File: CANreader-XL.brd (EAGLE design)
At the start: 99.8 x 49.8 mm, 101 parts, among them IC1 STM32F107RBT, IC2 TJA1055T/3, IC3 BD9G101G, IC4 LM1117IMPX-3.3, IC5 MCP2562-SOIC8, IC7 DP83848I, Q1 25MHz, SW1 SLEEP, SW2 TERM, U1 HC_05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

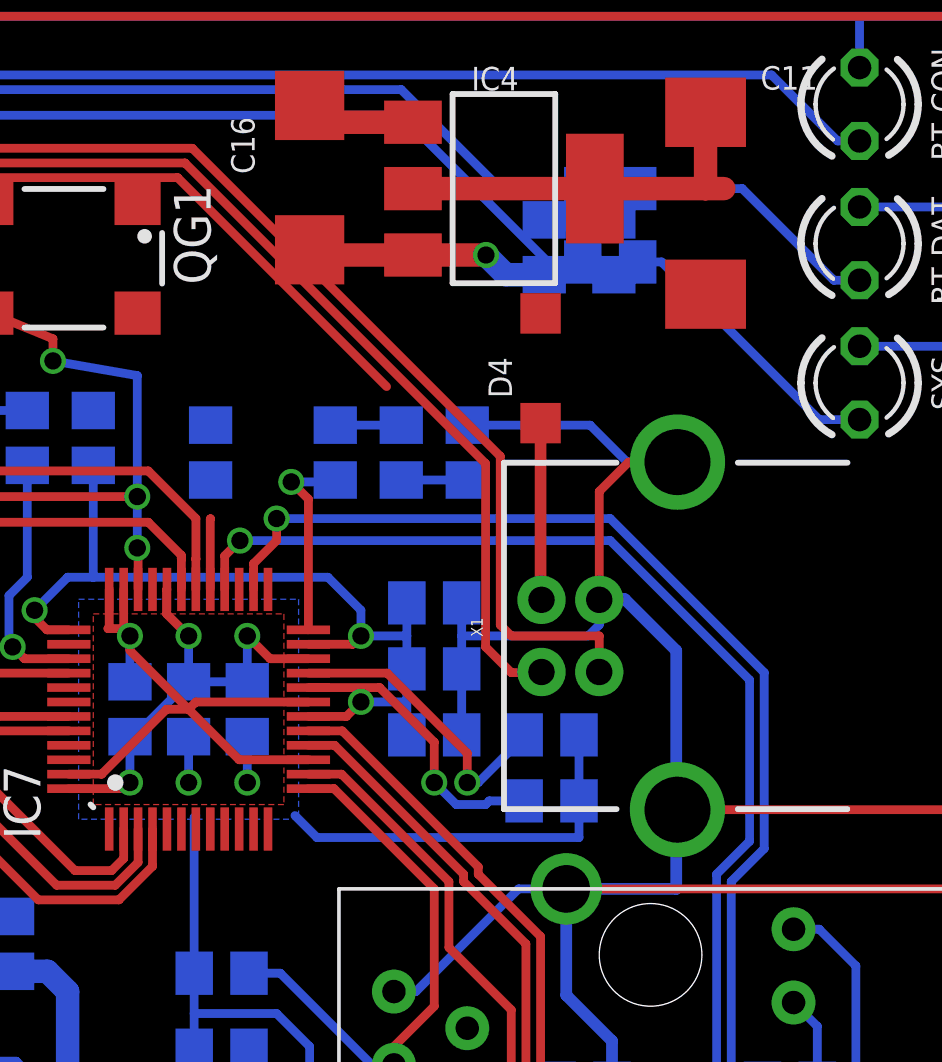
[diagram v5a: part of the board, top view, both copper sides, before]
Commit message: USB VDD capacitor
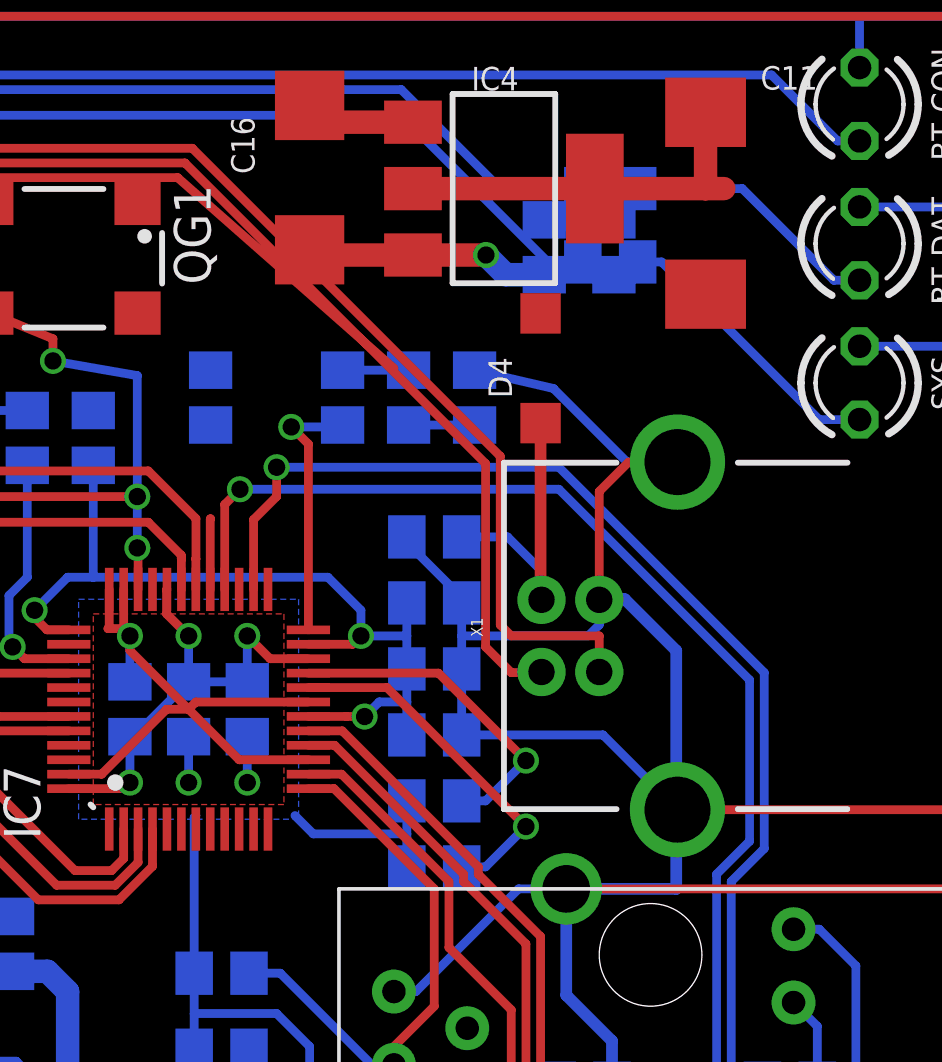
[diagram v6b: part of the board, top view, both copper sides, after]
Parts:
- added C41: 1mF, rcl:C0805
- moved R30 4.66 mm to (81.4, 19.6), turned to 0 degrees
- moved R31 4.66 mm to (81.4, 21.8), turned to 0 degrees
- moved R32 1.92 mm to (78.2, 35.8)
- moved R33 1.92 mm to (80.5, 35.8)
- moved R34 1.92 mm to (82.8, 35.8)
- moved R18 1.91 mm to (73.7, 35.8)
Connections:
- net GND: now also C41.2
- net USB_VBUS: now also C41.1
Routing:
- net GND: track 942.6 -> 954.5 mm
- net +3V3: track 309.7 -> 302.4 mm
- net USB_VBUS: track 38.8 -> 42.8 mm
- net LED_LINK: track 39.7 -> 42.2 mm
- net LEDACT_LINK: track 37.5 -> 40.0 mm
- net N$17: track 10.0 -> 12.3 mm
- net N$26: track 6.92 -> 9.08 mm
- net N$21: track 10.4 -> 11.6 mm

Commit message: Change connector, route
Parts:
- removed JP1: BOOT, pinhead:1X03
- removed X3: CAN+GPIO, con-molex-micro-fit-3_0:43045-1200
- removed X4: UART, con-molex-micro-fit-3_0:43045-0400
- added JP2: BOOT, STM32_CAN-USB:1X03
- added X5: (no value), con-molex-micro-fit-3_0:43045-1600
- moved C31 31.4 mm to (68.3, 25.0), flipped to the bottom
- moved R10 17.5 mm to (67.1, 34.4), turned to 90 degrees
- moved R19 13.3 mm to (63.4, 21.2), turned to 90 degrees
- moved R20 13.3 mm to (65.9, 21.2), turned to 90 degrees
- moved R5 11.9 mm to (40.3, 33.4)
- moved R23 5.31 mm to (40.3, 30.9), turned to 180 degrees
- moved R12 4.65 mm to (40.3, 38.5)
- moved R11 4.51 mm to (40.3, 35.9)
- moved R22 4.26 mm to (16.9, 5.97), turned to 180 degrees
- moved R6 4.02 mm to (36.3, 28.7), flipped to the top, turned to 90 degrees
- moved C1 0.76 mm to (50.0, 22.7)
- moved C2 0.76 mm to (52.6, 22.7)
- moved C3 0.76 mm to (55.1, 22.7)
- moved Q1 0.76 mm to (51.3, 22.7)
- moved X2 0.51 mm to (33.5, 40.3)
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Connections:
- removed net PA3: IC1.17, X3.P$11
- removed net PA4: IC1.20, X3.P$12
- removed net PA5: IC1.21, X3.P$5
- removed net PA6: IC1.22, X3.P$6
- new net PC14: IC1.3, X5.P$10
- new net PC15: IC1.4, X5.P$9
- new net PC2: IC1.10, X5.P$2
- new net PC3: IC1.11, X5.P$1
- net +12V: now also X5.P$12; no longer X3.P$7
- net +3V3: now also JP2.3, X5.P$11, X5.P$16; no longer JP1.3, X3.P$10, X4.P$3
- net CAN1H: now also X5.P$14; no longer X3.P$9
- net CAN1L: now also X5.P$6; no longer X3.P$3
- net CAN2H: now also X5.P$13; no longer X3.P$8
- net CAN2L: now also X5.P$5; no longer X3.P$2
- net GND: now also JP2.1, X5.P$3, X5.P$4, X5.P$8; no longer JP1.1, X3.P$1, X3.P$4, X4.P$1
- net N$29: now also JP2.2; no longer JP1.2
- net UART5_RX: now also X5.P$15; no longer X4.P$4
- net UART5_TX: now also X5.P$7; no longer X4.P$2
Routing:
- net PC3: track 0.00 -> 72.4 mm, vias 0 -> 3
- net PC2: track 0.00 -> 70.8 mm, vias 0 -> 3
- net PC14: track 0.00 -> 60.1 mm, vias 0 -> 1
- net PC15: track 0.00 -> 59.4 mm, vias 0 -> 1
- net EN: track 8.95 -> 54.0 mm, vias 0 -> 2
- net CAN2_STBY: track 6.39 -> 45.8 mm, vias 0 -> 2
- net TJA_INH: track 49.0 -> 20.9 mm, vias 1 -> 2
- net N$3: track 0.00 -> 12.2 mm
- net CAN2L: track 18.4 -> 29.7 mm, vias 0 -> 1
- net CAN2H: track 18.4 -> 28.5 mm
- net N$4: track 0.00 -> 9.98 mm, vias 0 -> 1
- net +12V: track 32.2 -> 41.7 mm, vias 0 -> 1
- net GND: track 954.5 -> 963.7 mm, vias 11 -> 12
- net CAN1L: track 24.0 -> 14.8 mm
- net BAT: track 48.1 -> 56.6 mm, vias 1 -> 2
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
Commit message: Route
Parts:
- D3: device STM32_CAN-USB:DO214AA -> diode:SMBJ
- Q1: device crystal:HC49UP -> crystal:HC49/S
- moved D1 31.6 mm to (44.6, 22.2), turned to 180 degrees
- moved R7 30.7 mm to (36.7, 20.2), turned to 90 degrees
- moved C12 30.0 mm to (39.8, 19.1), turned to 270 degrees
- moved R8 29.6 mm to (39.2, 20.2), turned to 90 degrees
- moved C13 28.9 mm to (41.8, 20.2), turned to 270 degrees
- moved IC3 28.8 mm to (37.8, 17.7), turned to 180 degrees
- moved C14 28.2 mm to (33.0, 14.1)
- moved DR2 23.0 mm to (43.4, 17.5), turned to 270 degrees
- moved C15 13.5 mm to (50.2, 17.5), turned to 0 degrees
- moved D4 12.1 mm to (73.0, 38.0), turned to 0 degrees
- moved R10 11.2 mm to (57.4, 40.1), turned to 180 degrees
- moved R19 11.0 mm to (53.1, 25.0)
- moved R20 11.0 mm to (55.6, 25.0)
- moved C32 10.5 mm to (59.3, 32.3)
- moved R30 10.2 mm to (71.2, 18.8)
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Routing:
- net EN: track 54.0 -> 16.4 mm, vias 2 -> 0
- net +5V: track 85.6 -> 115.0 mm, vias 5 -> 6
- net +3V3: track 308.6 -> 332.4 mm, vias 10 -> 13
- net GND: track 963.7 -> 985.5 mm, vias 12 -> 16
- net N$33: track 80.8 -> 72.3 mm
- net RMII_REF_CLK: track 31.9 -> 24.5 mm
- net RMII_MDIO: track 22.8 -> 15.5 mm
- net HC_RESET: track 50.6 -> 43.5 mm
- net SWDIO: track 18.5 -> 11.7 mm
- net N$4: track 9.98 -> 4.02 mm
- net HC_KEY: track 49.0 -> 43.2 mm
- net RMII_MDC: track 25.4 -> 20.0 mm
- net N$11: track 9.00 -> 3.62 mm
- net RMII_TXD1: track 38.4 -> 43.7 mm
- net RMII_TXD0: track 34.9 -> 40.0 mm
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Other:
- board size 99.8 x 49.8 mm -> 89.7 x 49.8 mm
